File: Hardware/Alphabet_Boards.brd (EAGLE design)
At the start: 57.7 x 52.8 mm, 113 parts

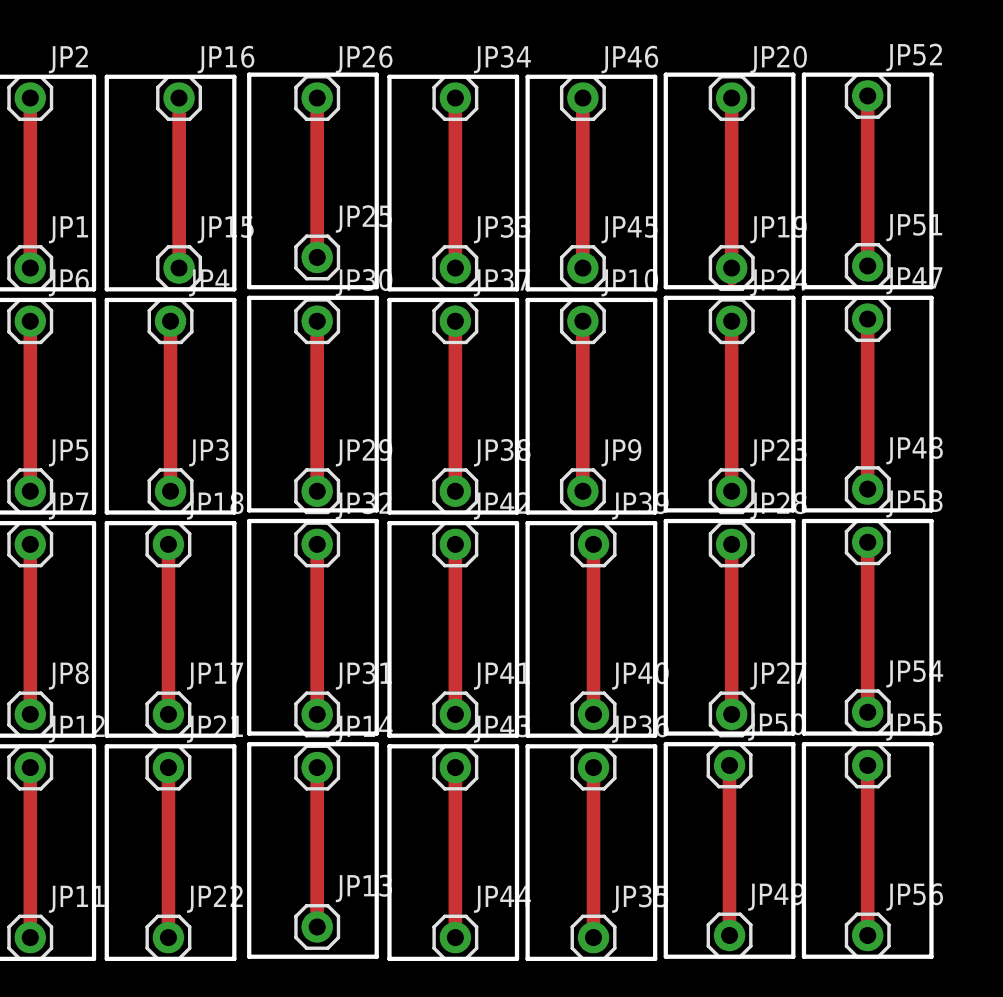
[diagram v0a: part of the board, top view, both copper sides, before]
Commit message: Rearranging for grid line panelization.
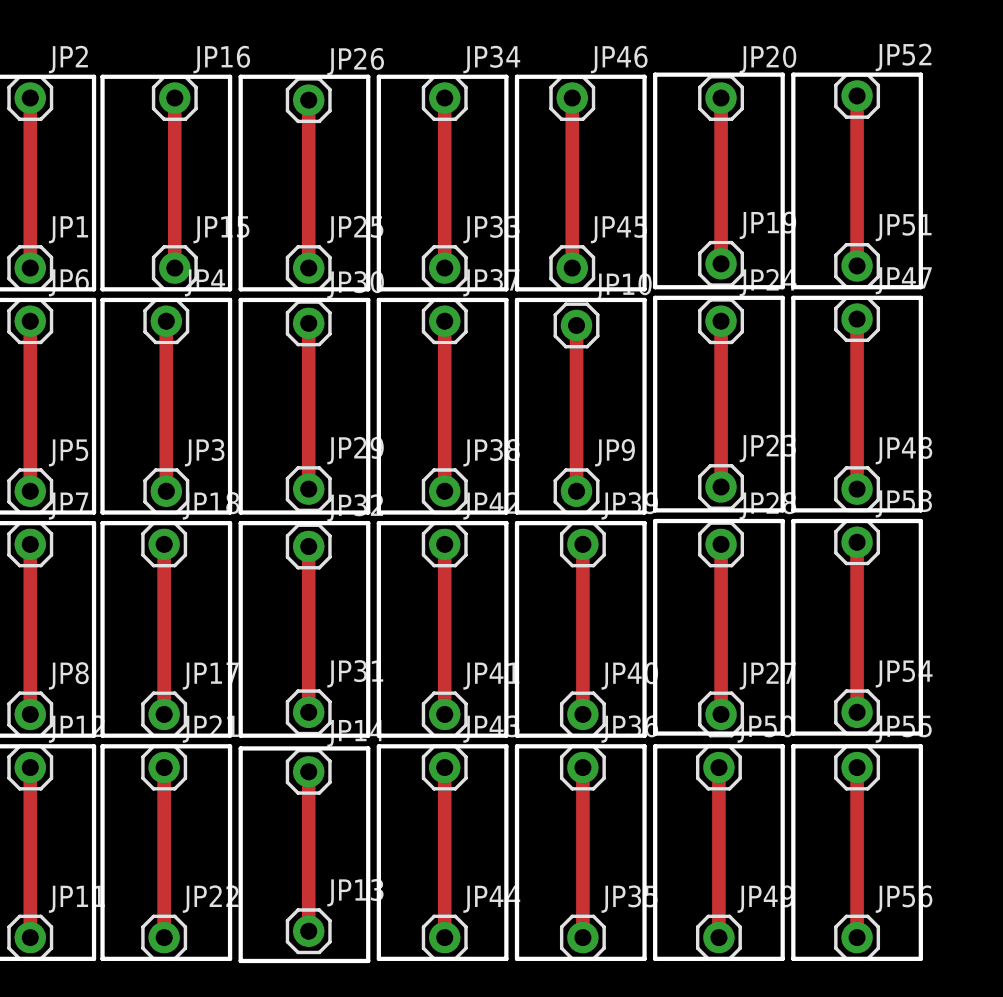
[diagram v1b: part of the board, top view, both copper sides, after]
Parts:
- moved JP25 0.81 mm to (20.4, 41.3)
- moved JP19 0.68 mm to (45.1, 41.5)
- moved JP23 0.68 mm to (45.1, 28.2)
- moved JP50 0.65 mm to (45.0, 11.4)
- moved JP49 0.65 mm to (45.0, 1.27)
- moved JP55 0.65 mm to (53.2, 11.4)
- moved LOGO55 0.65 mm to (45.1, 4.32)
- moved JP56 0.65 mm to (53.2, 1.27)
- moved LOGO1 0.65 mm to (53.2, 4.95)
- moved LOGO19 0.65 mm to (54.4, 6.99)
- moved LOGO2 0.65 mm to (46.2, 6.99)
- moved JP35 0.64 mm to (36.8, 1.27)
- moved JP36 0.64 mm to (36.8, 11.4)
- moved JP39 0.64 mm to (36.8, 24.8)
- moved JP40 0.64 mm to (36.8, 14.6)
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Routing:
- net N$18: track 10.8 -> 10.3 mm
- net N$8: track 9.53 -> 10.0 mm
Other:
- board size 57.7 x 52.8 mm -> 57 x 53 mm

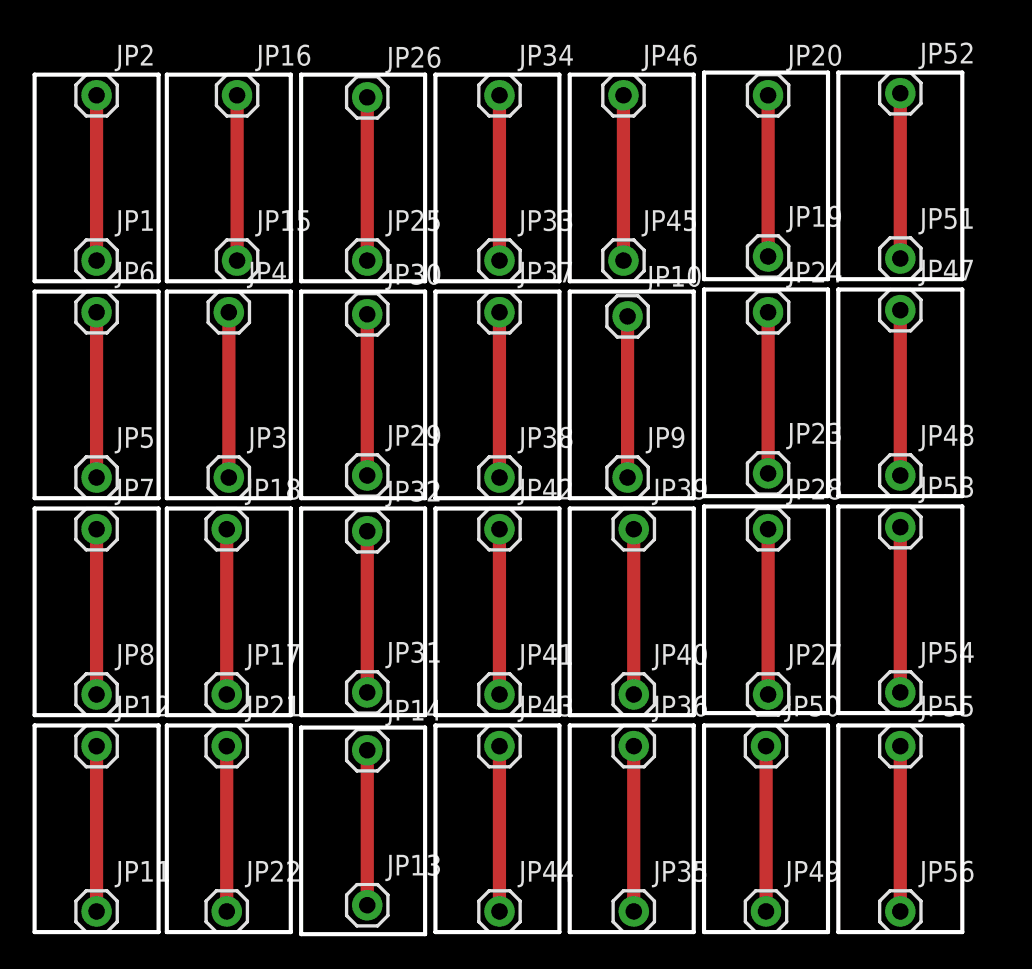
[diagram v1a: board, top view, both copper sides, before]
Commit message: Updating letter boards to be blank
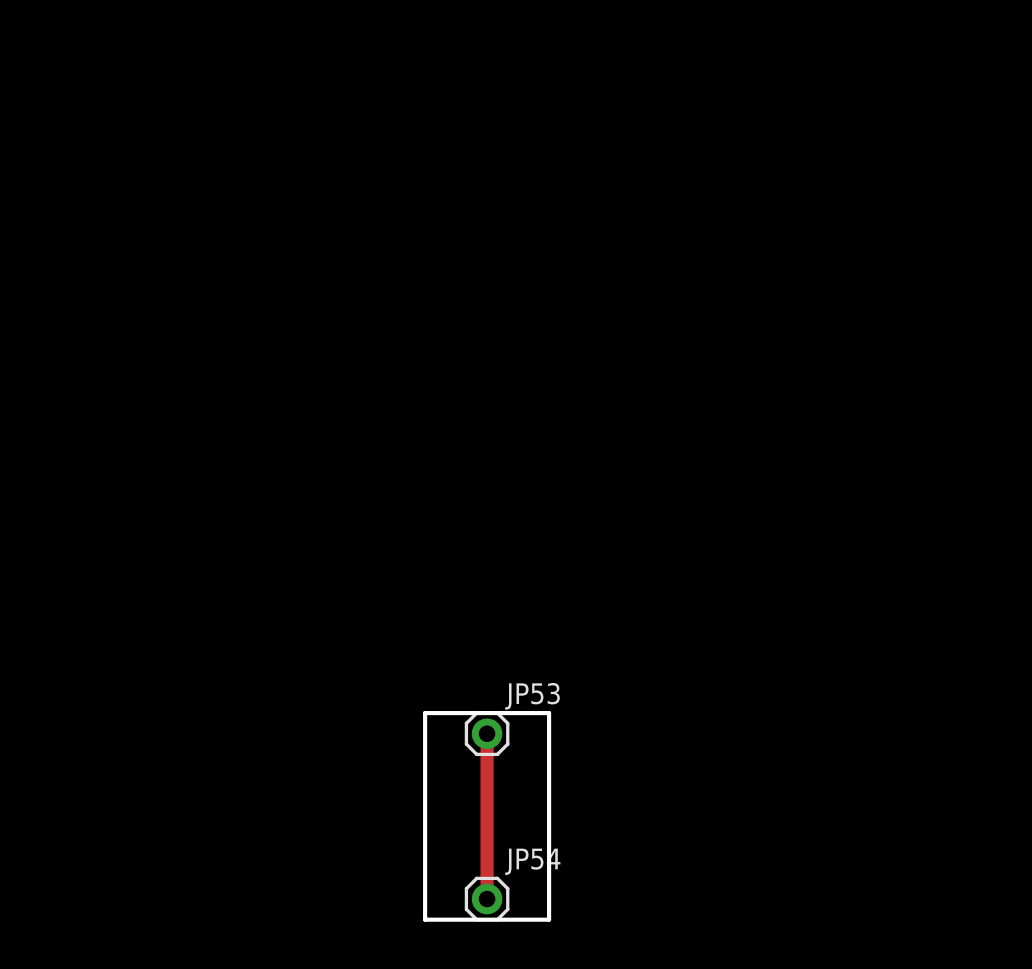
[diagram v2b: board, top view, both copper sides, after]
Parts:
- removed JP1, JP10, JP11, JP12, JP13, JP14, JP15, JP16, JP17, JP18, JP19, JP2, JP20, JP21, JP22, JP23, JP24, JP25, JP26, JP27, JP28, JP29, JP3, JP30, JP31, JP32, JP33, JP34, JP35, JP36, JP37, JP38, JP39, JP4, JP40, JP41, JP42, JP43, JP44, JP45, JP46, JP47, JP48, JP49, JP5, JP50, JP51, JP52, JP55, JP56, JP6, JP7, JP8, JP9: M01PTH, SparkFun-Connectors:1X01
- removed LOGO1, LOGO29, LOGO30, LOGO31, LOGO32, LOGO33, LOGO34, LOGO35, LOGO36, LOGO37, LOGO38, LOGO39, LOGO40, LOGO41, LOGO42, LOGO43, LOGO44, LOGO45, LOGO46, LOGO47, LOGO48, LOGO50, LOGO51, LOGO52, LOGO53, LOGO54, LOGO55: OSHW-LOGOS, SparkFun-Aesthetics:OSHW-LOGO-S
- removed LOGO10, LOGO11, LOGO12, LOGO13, LOGO14, LOGO15, LOGO16, LOGO17, LOGO18, LOGO19, LOGO2, LOGO20, LOGO21, LOGO22, LOGO24, LOGO25, LOGO26, LOGO27, LOGO28, LOGO3, LOGO4, LOGO5, LOGO56, LOGO6, LOGO7, LOGO8, LOGO9: SFE_LOGO_FLAME.1_INCH, SparkFun-Aesthetics:SFE_LOGO_FLAME_.1
- moved JP53 28.4 mm to (27.8, 12.2)
- moved JP54 28.4 mm to (27.8, 2.03)
- moved LOGO23 28.4 mm to (29.0, 7.62)
- moved LOGO49 28.4 mm to (27.7, 5.59)
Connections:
- removed net N$1: JP1.1, JP2.1
- removed net N$10: JP31.1, JP32.1
- removed net N$11: JP13.1, JP14.1
- removed net N$12: JP37.1, JP38.1
- removed net N$13: JP41.1, JP42.1
- removed net N$14: JP43.1, JP44.1
- removed net N$15: JP45.1, JP46.1
- removed net N$16: JP10.1, JP9.1
- removed net N$17: JP35.1, JP36.1
- removed net N$18: JP19.1, JP20.1
- removed net N$19: JP23.1, JP24.1
- removed net N$2: JP5.1, JP6.1
- removed net N$20: JP27.1, JP28.1
- removed net N$21: JP51.1, JP52.1
- removed net N$22: JP47.1, JP48.1
- removed net N$23: JP17.1, JP18.1
- removed net N$24: JP33.1, JP34.1
- removed net N$25: JP39.1, JP40.1
- removed net N$26: JP49.1, JP50.1
- removed net N$28: JP55.1, JP56.1
- removed net N$3: JP7.1, JP8.1
- removed net N$4: JP11.1, JP12.1
- removed net N$5: JP15.1, JP16.1
- removed net N$6: JP3.1, JP4.1
- removed net N$7: JP21.1, JP22.1
- removed net N$8: JP25.1, JP26.1
- removed net N$9: JP29.1, JP30.1
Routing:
- net N$18: track 10.3 -> 0.00 mm
- net N$5: track 10.2 -> 0.00 mm
- net N$24: track 10.2 -> 0.00 mm
- net N$15: track 10.2 -> 0.00 mm
- net N$1: track 10.2 -> 0.00 mm
- net N$7: track 10.2 -> 0.00 mm
- net N$6: track 10.2 -> 0.00 mm
- net N$4: track 10.2 -> 0.00 mm
- net N$3: track 10.2 -> 0.00 mm
- net N$28: track 10.2 -> 0.00 mm
- net N$26: track 10.2 -> 0.00 mm
- net N$25: track 10.2 -> 0.00 mm
- net N$23: track 10.2 -> 0.00 mm
- net N$20: track 10.2 -> 0.00 mm
- net N$2: track 10.2 -> 0.00 mm
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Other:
- board size 57 x 53 mm -> 7.6 x 12.7 mm
- board text removed: "A"
- board text removed: "B"
- board text removed: "C"
- board text removed: "D"
- board text removed: "E"
- board text removed: "F"
- board text removed: "G"
- board text removed: "H"
- board text removed: "I"
- board text removed: "J"
- board text removed: "K"
- board text removed: "L"
- board text removed: "M"
- board text removed: "N"
- board text removed: "O"
- board text removed: "P"
- board text removed: "Q"
- board text removed: "R"
- board text removed: "S"
- board text removed: "T"
- board text removed: "U"
- board text removed: "V"
- board text removed: "W"
- board text removed: "X"
- board text removed: "Y"
- board text removed: "Z"

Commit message: Updating to Scrabble distribution
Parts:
- removed JP53, JP54: M01PTH, SparkFun-Connectors:1X01
- added LOGO1, LOGO101, LOGO103, LOGO105, LOGO107, LOGO109, LOGO11, LOGO111, LOGO113, LOGO115, LOGO117, LOGO119, LOGO121, LOGO123, LOGO125, LOGO127, LOGO129, LOGO13, LOGO131, LOGO133, LOGO135, LOGO137, LOGO139, LOGO141, LOGO143, LOGO145, LOGO147, LOGO149, LOGO15, LOGO151, LOGO153, LOGO155, LOGO157, LOGO159, LOGO161, LOGO163, LOGO165, LOGO167, LOGO169, LOGO17, LOGO171, LOGO173, LOGO175, LOGO177, LOGO179, LOGO181, LOGO183, LOGO185, LOGO187, LOGO189, LOGO19, LOGO191, LOGO193, LOGO195, LOGO197, LOGO199, LOGO21, LOGO24, LOGO26, LOGO28, LOGO3, LOGO30, LOGO32, LOGO34, LOGO36, LOGO38, LOGO40, LOGO42, LOGO44, LOGO46, LOGO48, LOGO5, LOGO51, LOGO53, LOGO55, LOGO57, LOGO59, LOGO61, LOGO63, LOGO65, LOGO67, LOGO69, LOGO7, LOGO71, LOGO73, LOGO75, LOGO77, LOGO79, LOGO81, LOGO83, LOGO85, LOGO87, LOGO89, LOGO9, LOGO91, LOGO93, LOGO95, LOGO97, LOGO99: SFE_LOGO_FLAME.1_INCH, SparkFun-Aesthetics:SFE_LOGO_FLAME_.1
- added LOGO10, LOGO100, LOGO102, LOGO104, LOGO106, LOGO108, LOGO110, LOGO112, LOGO114, LOGO116, LOGO118, LOGO12, LOGO120, LOGO122, LOGO124, LOGO126, LOGO128, LOGO130, LOGO132, LOGO134, LOGO136, LOGO138, LOGO14, LOGO140, LOGO142, LOGO144, LOGO146, LOGO148, LOGO150, LOGO152, LOGO154, LOGO156, LOGO158, LOGO16, LOGO160, LOGO162, LOGO164, LOGO166, LOGO168, LOGO170, LOGO172, LOGO174, LOGO176, LOGO178, LOGO18, LOGO180, LOGO182, LOGO184, LOGO186, LOGO188, LOGO190, LOGO192, LOGO194, LOGO196, LOGO198, LOGO2, LOGO20, LOGO200, LOGO22, LOGO25, LOGO27, LOGO29, LOGO31, LOGO33, LOGO35, LOGO37, LOGO39, LOGO4, LOGO41, LOGO43, LOGO45, LOGO47, LOGO50, LOGO52, LOGO54, LOGO56, LOGO58, LOGO6, LOGO60, LOGO62, LOGO64, LOGO66, LOGO68, LOGO70, LOGO72, LOGO74, LOGO76, LOGO78, LOGO8, LOGO80, LOGO82, LOGO84, LOGO86, LOGO88, LOGO90, LOGO92, LOGO94, LOGO96, LOGO98: OSHW-LOGOS, SparkFun-Aesthetics:OSHW-LOGO-S
- added U$1, U$10, U$100, U$11, U$12, U$13, U$14, U$15, U$16, U$17, U$18, U$19, U$2, U$20, U$21, U$22, U$23, U$24, U$25, U$26, U$27, U$28, U$29, U$3, U$30, U$31, U$32, U$33, U$34, U$35, U$36, U$37, U$38, U$39, U$4, U$40, U$41, U$42, U$43, U$44, U$45, U$46, U$47, U$48, U$49, U$5, U$50, U$51, U$52, U$53, U$54, U$55, U$56, U$57, U$58, U$59, U$6, U$60, U$61, U$62, U$63, U$64, U$65, U$66, U$67, U$68, U$69, U$7, U$70, U$71, U$72, U$73, U$74, U$75, U$76, U$77, U$78, U$79, U$8, U$80, U$81, U$82, U$83, U$84, U$85, U$86, U$87, U$88, U$89, U$9, U$90, U$91, U$92, U$93, U$94, U$95, U$96, U$97, U$98, U$99: ALPHABET, Local Library:ALPHABET_BOARD
- FRAME1: value FRAME-LETTER -> FRAME-LEDGER
- moved FRAME1 31.8 mm to (34.3, -8.89)
- moved LOGO23 22.8 mm to (6.35, 10.3)
- moved LOGO49 22.6 mm to (5.08, 4.45)
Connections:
- removed net N$27: JP53.1, JP54.1
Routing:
- net N$27: track 10.2 -> 0.00 mm
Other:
- board size 7.6 x 12.7 mm -> 10.2 x 16.5 mm
- board text added: "A"
- board text added: "B"
- board text added: "C"
- board text added: "D"
- board text added: "E"
- board text added: "F"
- board text added: "G"
- board text added: "H"
- board text added: "I"
- board text added: "J"
- board text added: "K"
- board text added: "L"
- board text added: "M"
- board text added: "N"
- board text added: "O"
- board text added: "P"
- board text added: "Q"
- board text added: "R"
- board text added: "S"
- board text added: "T"
- board text added: "U"
- board text added: "V"
- board text added: "W"
- board text added: "X"
- board text added: "Y"
- board text added: "Z"

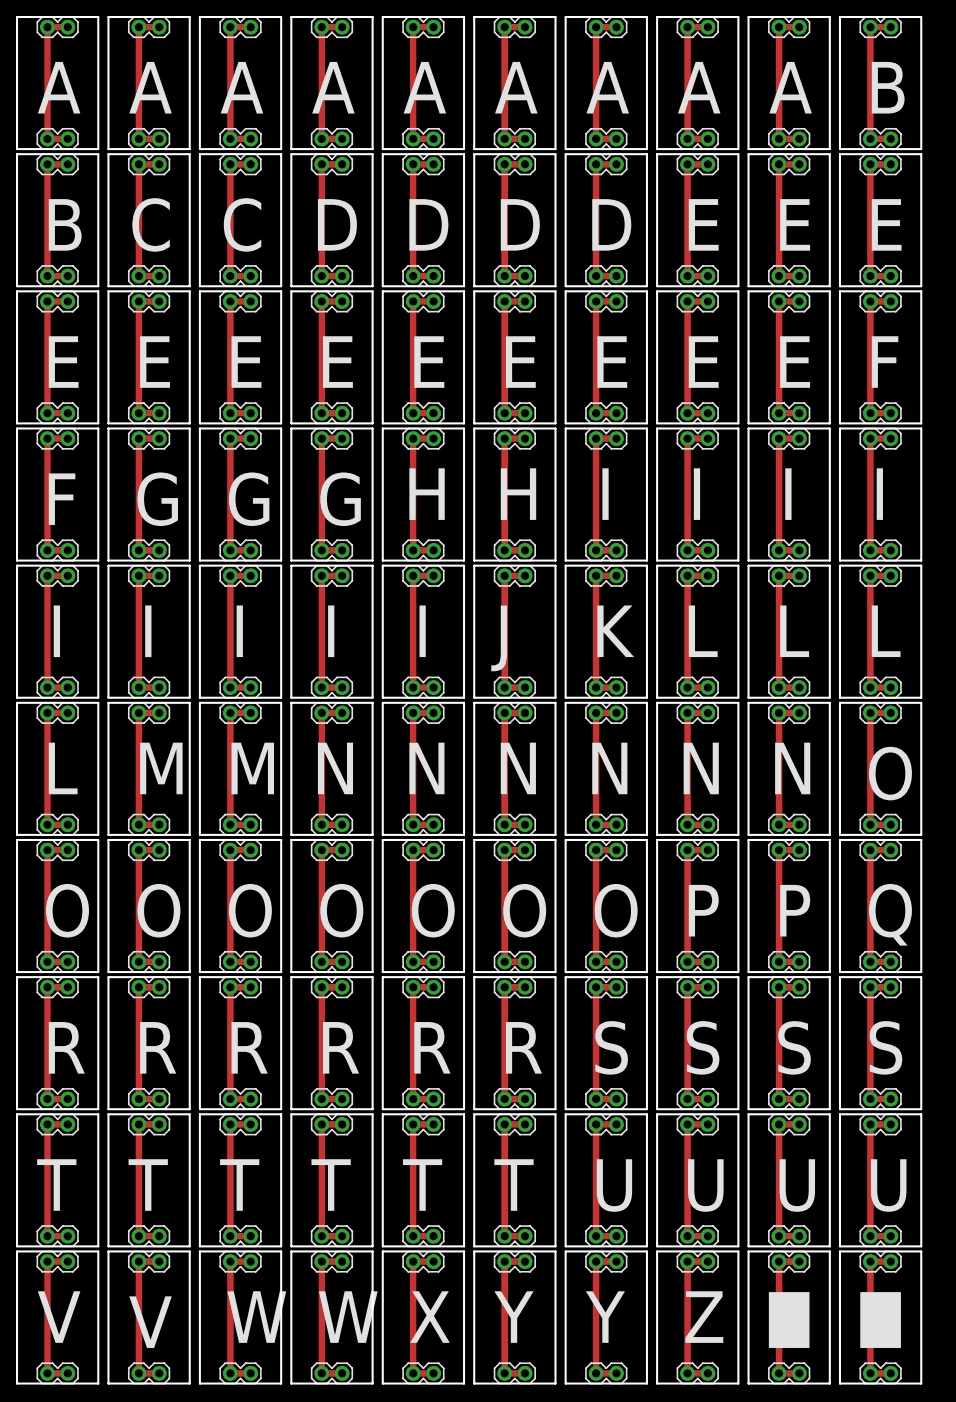
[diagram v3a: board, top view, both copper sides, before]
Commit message: re-did spacing for correct v-score
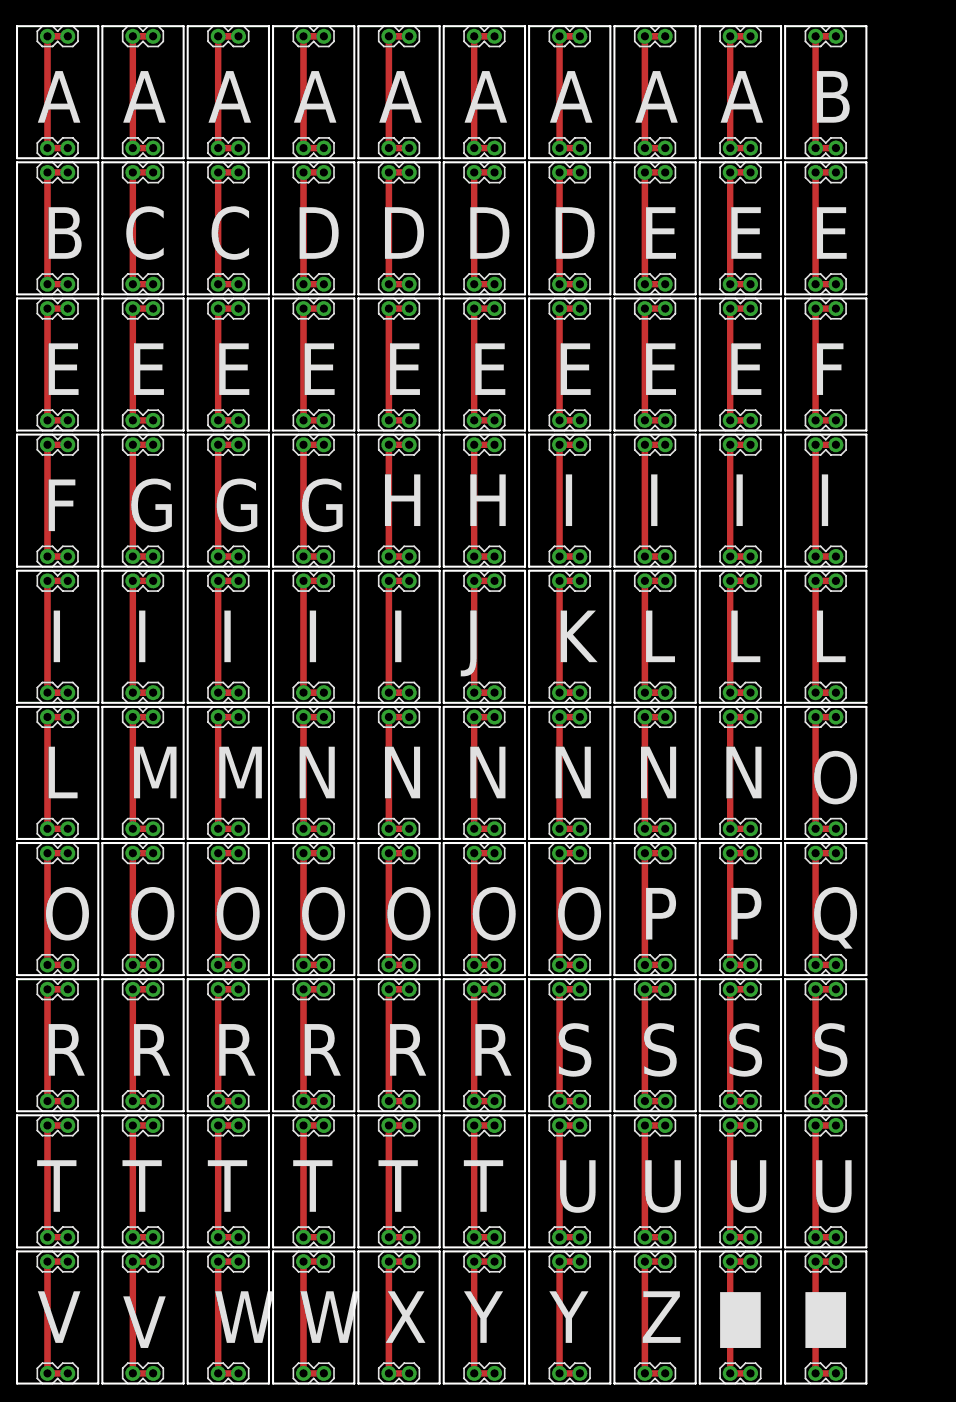
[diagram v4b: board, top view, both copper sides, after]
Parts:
- moved LOGO24 6.95 mm to (102.4, 163.4)
- moved LOGO25 6.95 mm to (101.1, 157.6)
- moved U$1 6.95 mm to (96.0, 153.2)
- moved LOGO185 6.93 mm to (102.4, 146.4)
- moved LOGO186 6.93 mm to (101.1, 140.6)
- moved U$76 6.93 mm to (96.0, 136.1)
- moved LOGO166 6.92 mm to (101.1, 123.6)
- moved U$25 6.92 mm to (96.0, 119.1)
- moved LOGO165 6.92 mm to (102.4, 129.4)
- moved LOGO145 6.90 mm to (102.4, 112.4)
- moved LOGO146 6.90 mm to (101.1, 106.6)
- moved U$26 6.90 mm to (96.0, 102.1)
- moved LOGO125 6.89 mm to (102.4, 95.4)
- moved LOGO126 6.89 mm to (101.1, 89.5)
- moved U$39 6.89 mm to (96.0, 85.1)
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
